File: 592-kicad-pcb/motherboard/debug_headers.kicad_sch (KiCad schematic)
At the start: 7 parts, among them J10 Conn_02x06_Odd_Even, J12 Conn_02x06_Odd_Even, J13 Conn_02x06_Odd_Even, J14 Conn_02x06_Odd_Even, J15 Conn_02x06_Odd_Even, J8 Conn_02x06_Odd_Even, J9 Conn_02x06_Odd_Even

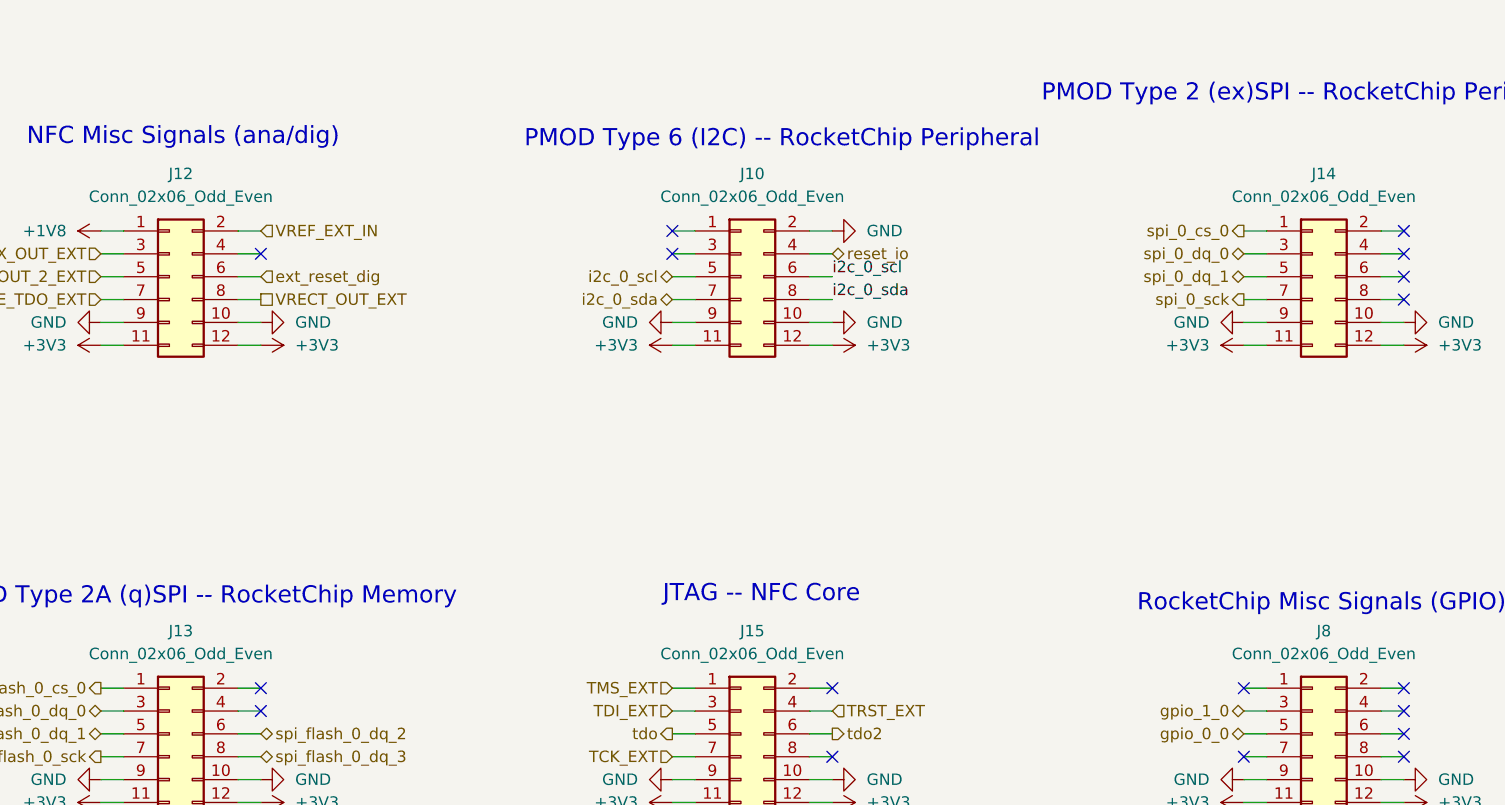
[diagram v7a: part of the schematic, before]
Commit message: combine hierarchy of all sans power
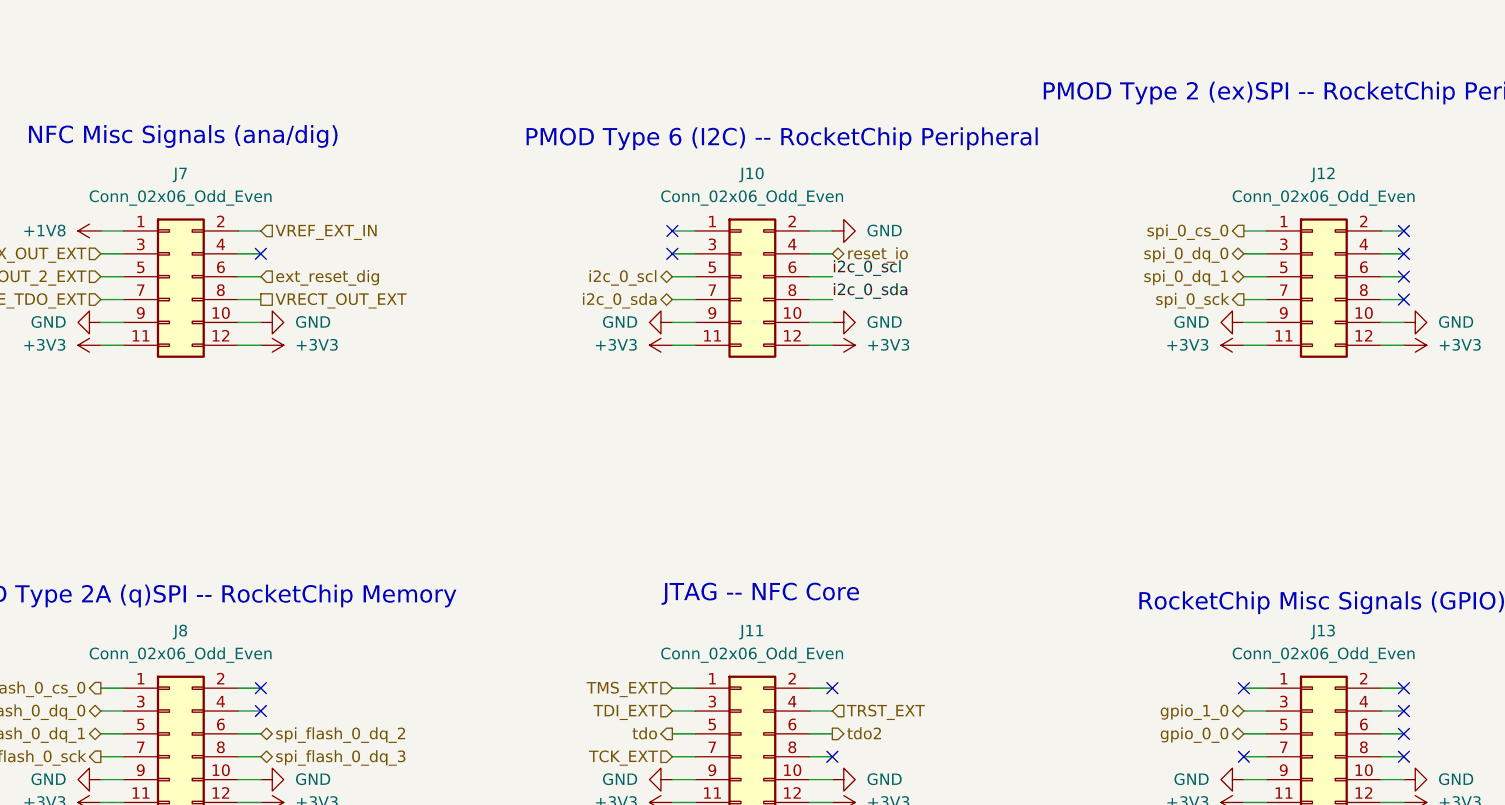
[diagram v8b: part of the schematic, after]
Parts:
- renumbered J15 to J11, J14 to J12, J8 to J13, J12 to J7, J13 to J8
